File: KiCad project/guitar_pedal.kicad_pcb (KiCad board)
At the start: 2 copper layers, 46 parts, among them J1 NMJ6HCD2, J2 NMJ6HCD2, J3 AVR-ISP-6, SW2 SWITCH_3PDT, U1 ATmega1284-P, U2 L7805, U3 TL061, U4 TL061, Y1 Crystal 16MHz

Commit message: Minor changes to PCB
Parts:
- moved C4 38.5 mm to (66.0, 48.2), turned to 0 degrees
- moved C2 31.4 mm to (66.0, 43.1), turned to 0 degrees
- moved D1 27.0 mm to (71.1, 38.0), turned to 180 degrees
- moved R1 24.3 mm to (66.0, 38.0), turned to 0 degrees
- moved C18 19.5 mm to (71.1, 31.5), turned to 90 degrees
- moved C3 15.6 mm to (66.0, 31.5), turned to -90 degrees
- moved C1 14.6 mm to (61.0, 31.5), turned to -90 degrees
- moved U2 8.13 mm to (66.0, 25.3), turned to 0 degrees
- moved C15 5.24 mm to (61.0, 38.1), turned to 90 degrees
- moved C8 3.80 mm to (45.7, 76.1)
- moved R2 3.80 mm to (45.7, 81.2)
- moved R6 2.66 mm to (29.2, 68.6)
- moved R3 1.26 mm to (45.7, 71.1)
- moved C9 1.26 mm to (45.7, 65.9)
- moved J3 0.32 mm to (38.1, 38.1)
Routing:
- net +5V: track 10.9 -> 180.4 mm
- net Net-(U4--): track 29.1 -> 63.8 mm
- net GND: track 0.00 -> 21.4 mm
- net PA0: track 73.3 -> 92.3 mm
- net Net-(U3--): track 10.8 -> 8.08 mm
- net Net-(SW2-C2): track 38.0 -> 36.7 mm
- net Net-(U1-AREF): track 6.20 -> 7.33 mm
- net Net-(J3-SCK): track 15.4 -> 14.5 mm
- net Net-(U3-+): track 36.0 -> 36.6 mm
- net Net-(U1-XTAL2): track 18.4 -> 17.9 mm

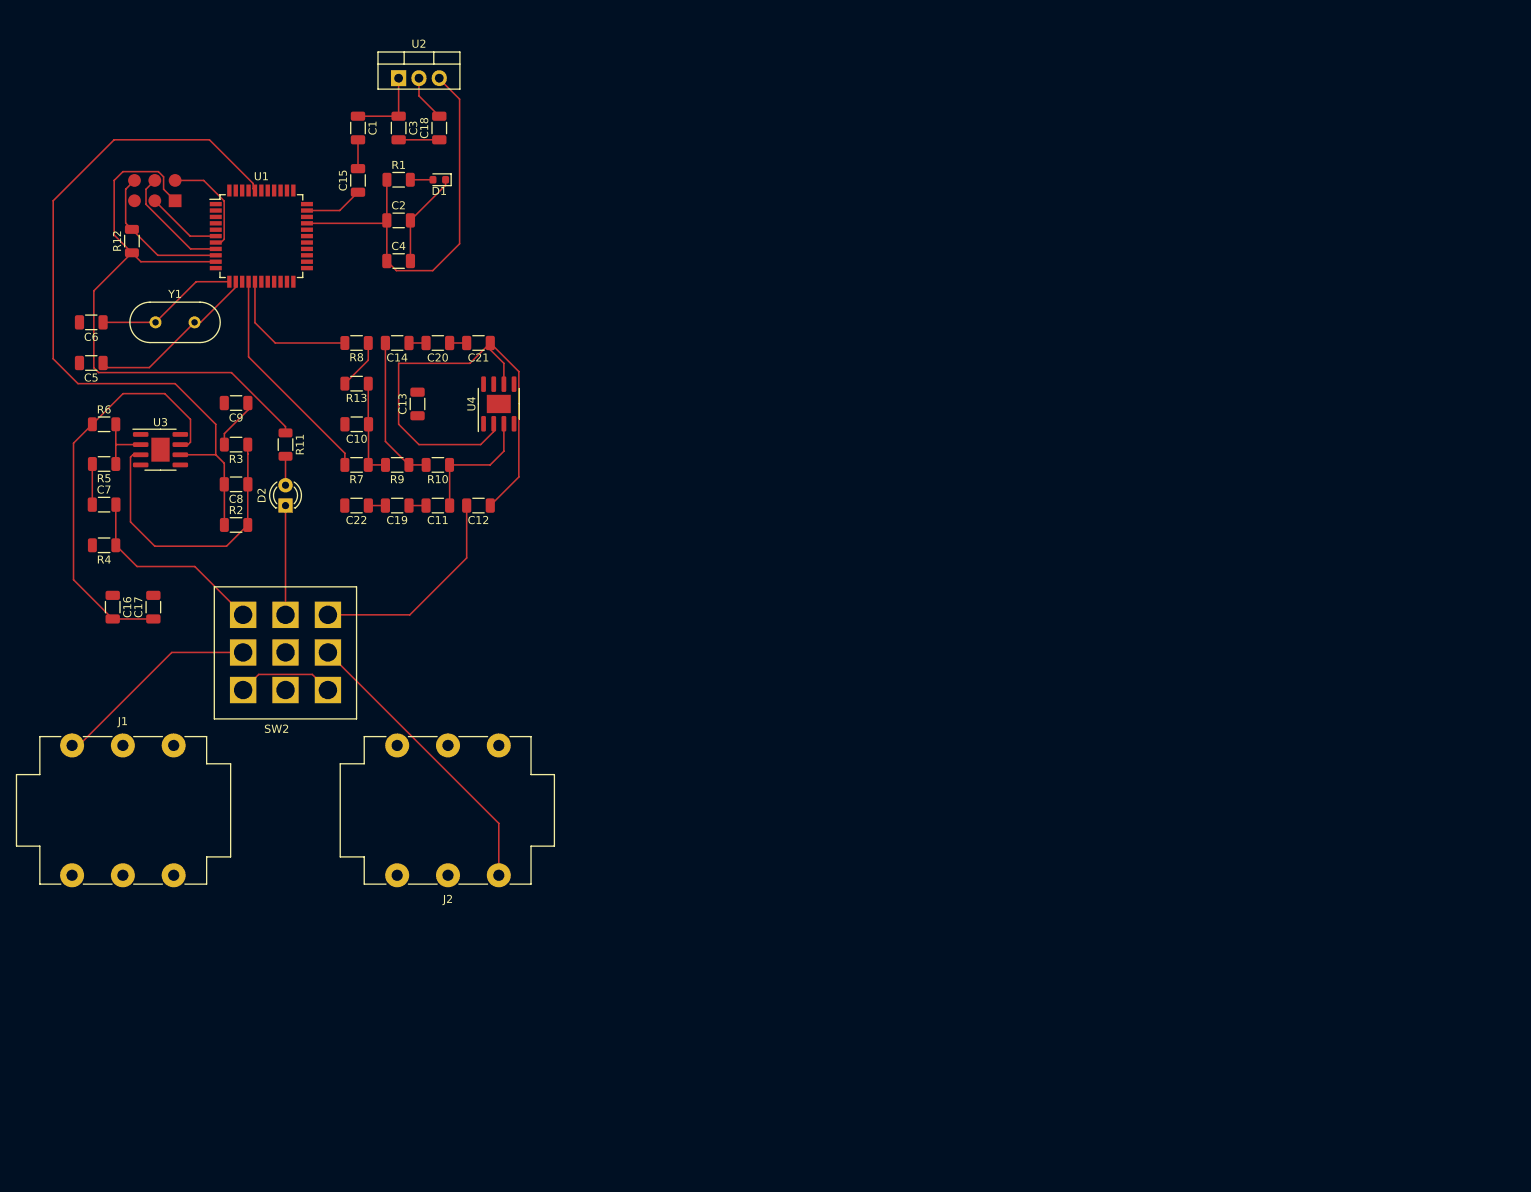
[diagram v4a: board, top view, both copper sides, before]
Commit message: Added remaining footprints to PCB, added ground plane and board edges.
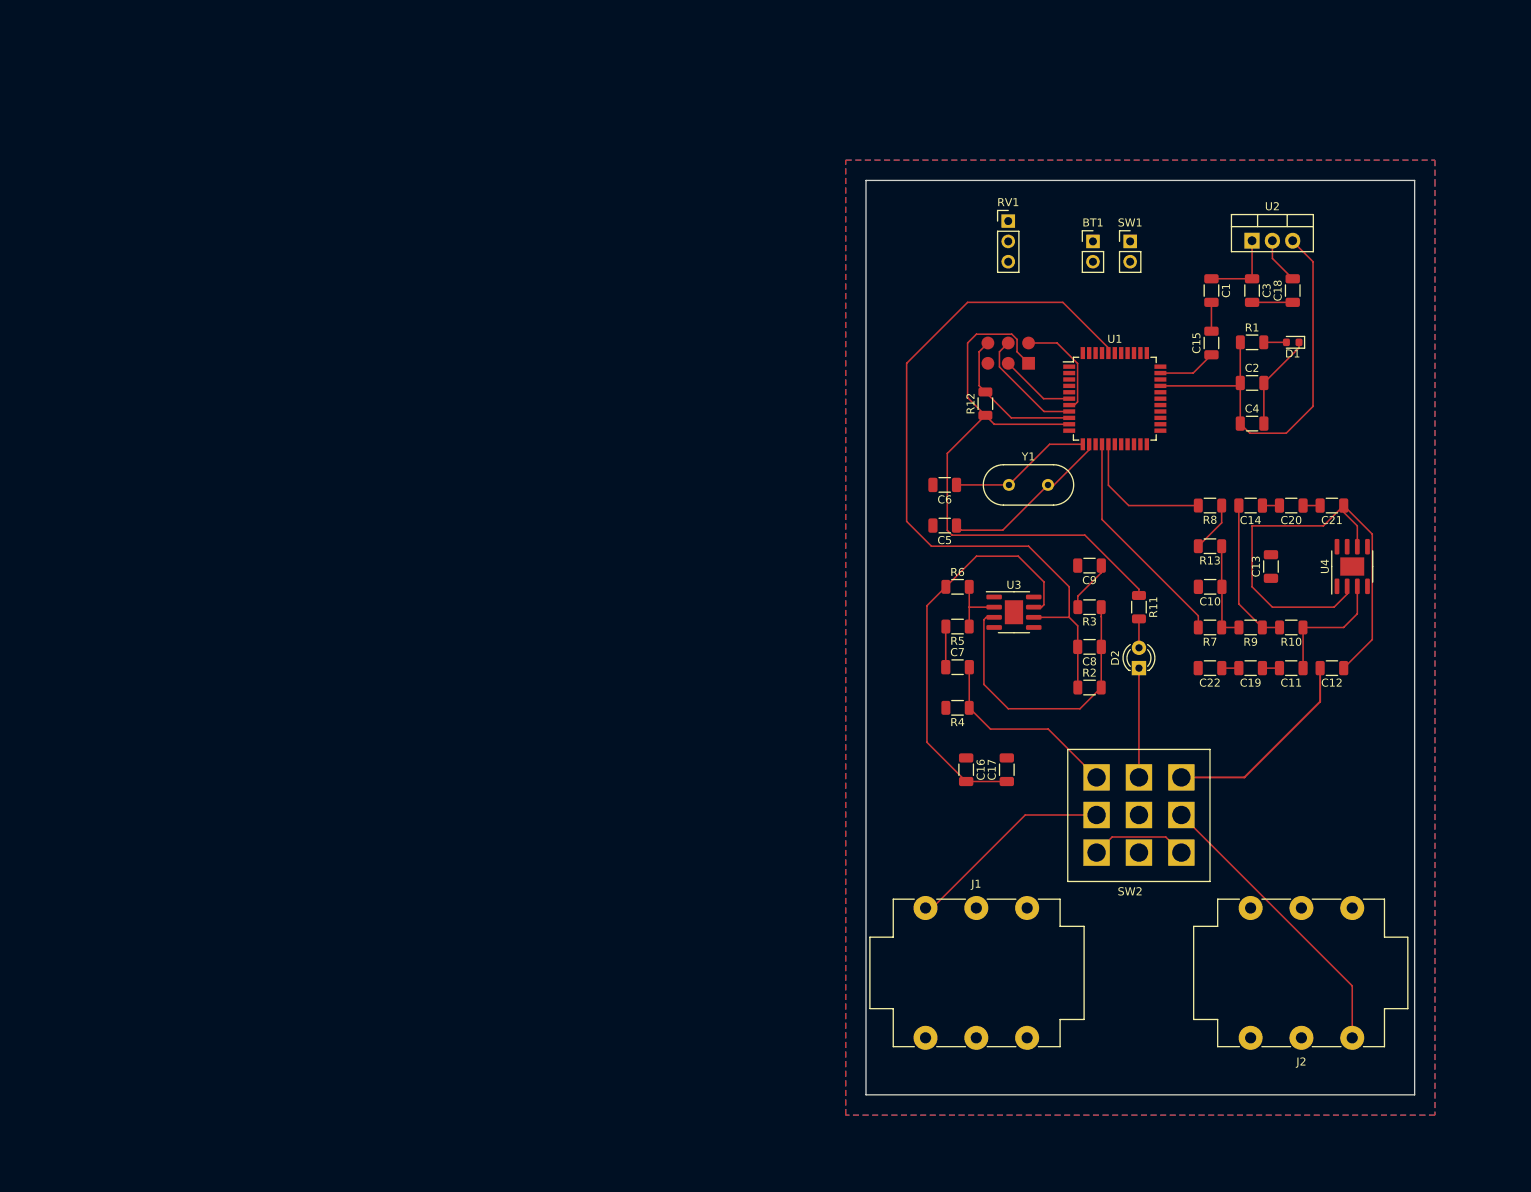
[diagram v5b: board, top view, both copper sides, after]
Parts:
- added BT1: 9V BATT, Connector_PinHeader_2.54mm:PinHeader_1x02_P2.54mm_Vertical, F.Cu at (152.8, 45.7)
- added RV1: R_Potentiometer, Connector_PinHeader_2.54mm:PinHeader_1x03_P2.54mm_Vertical, F.Cu at (142.2, 43.2)
- added SW1: SW_SPST, Connector_PinHeader_2.54mm:PinHeader_1x02_P2.54mm_Vertical, F.Cu at (157.5, 45.7)
- moved C11 108.6 mm to (177.6, 99.1)
- moved C13 108.6 mm to (175.1, 86.4)
- moved C17 108.6 mm to (142.1, 111.8)
- moved C18 108.6 mm to (177.8, 51.9)
- moved C20 108.6 mm to (177.6, 78.7)
- moved C22 108.6 mm to (167.5, 99.1)
- moved C5 108.6 mm to (134.3, 81.2)
- moved C6 108.6 mm to (134.3, 76.2)
- moved C7 108.6 mm to (135.9, 98.9)
- moved C8 108.6 mm to (152.4, 96.4)
- moved C9 108.6 mm to (152.4, 86.2)
- moved D1 108.6 mm to (177.8, 58.3)
- moved D2 108.6 mm to (158.6, 99.1)
- moved J1 108.6 mm to (131.9, 129.0)
- moved J2 108.6 mm to (185.2, 145.3)
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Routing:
- net FX Out: track 26.8 -> 25.5 mm
- added copper zone on B.Cu, net GND
- added copper zone on F.Cu, net GND
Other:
- board outline added: 68.6 x 114.3 mm

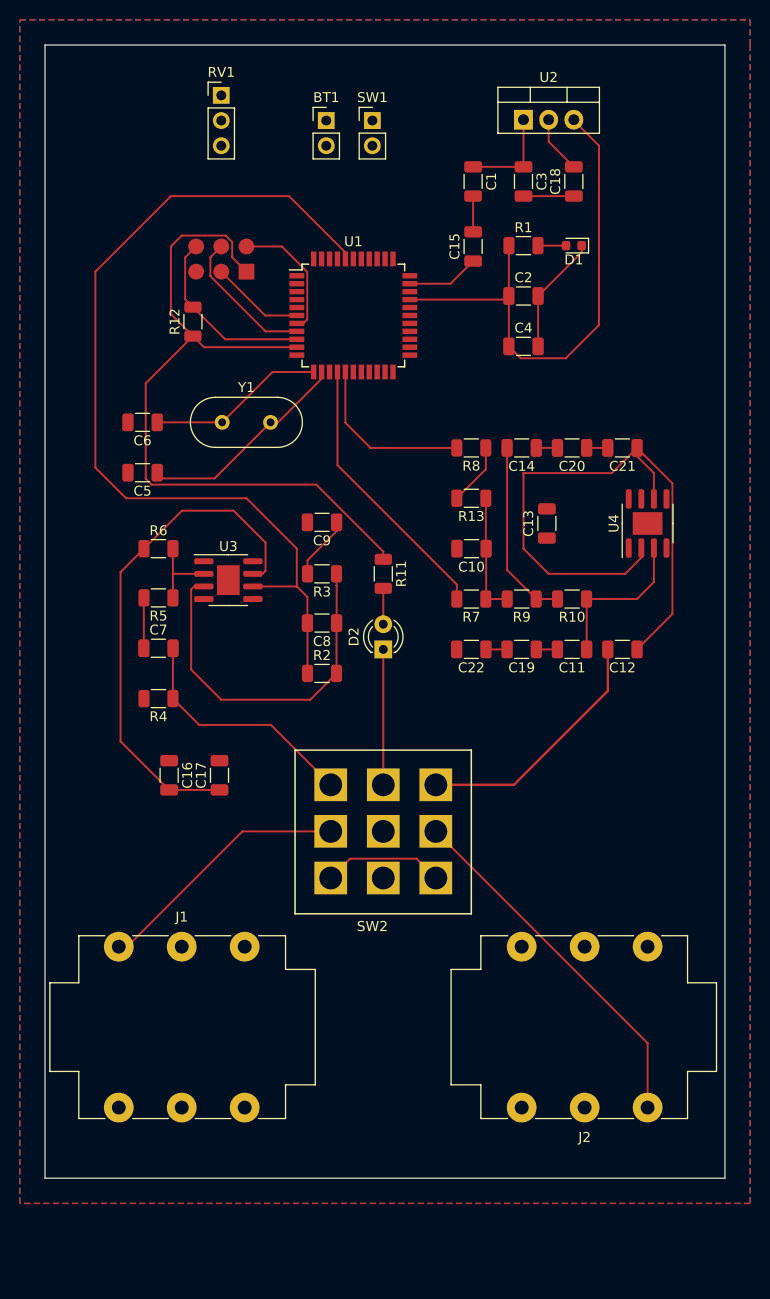
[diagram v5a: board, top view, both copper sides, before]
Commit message: Added second layer. All connections on board. No errors in DRC, 200+ warnings.
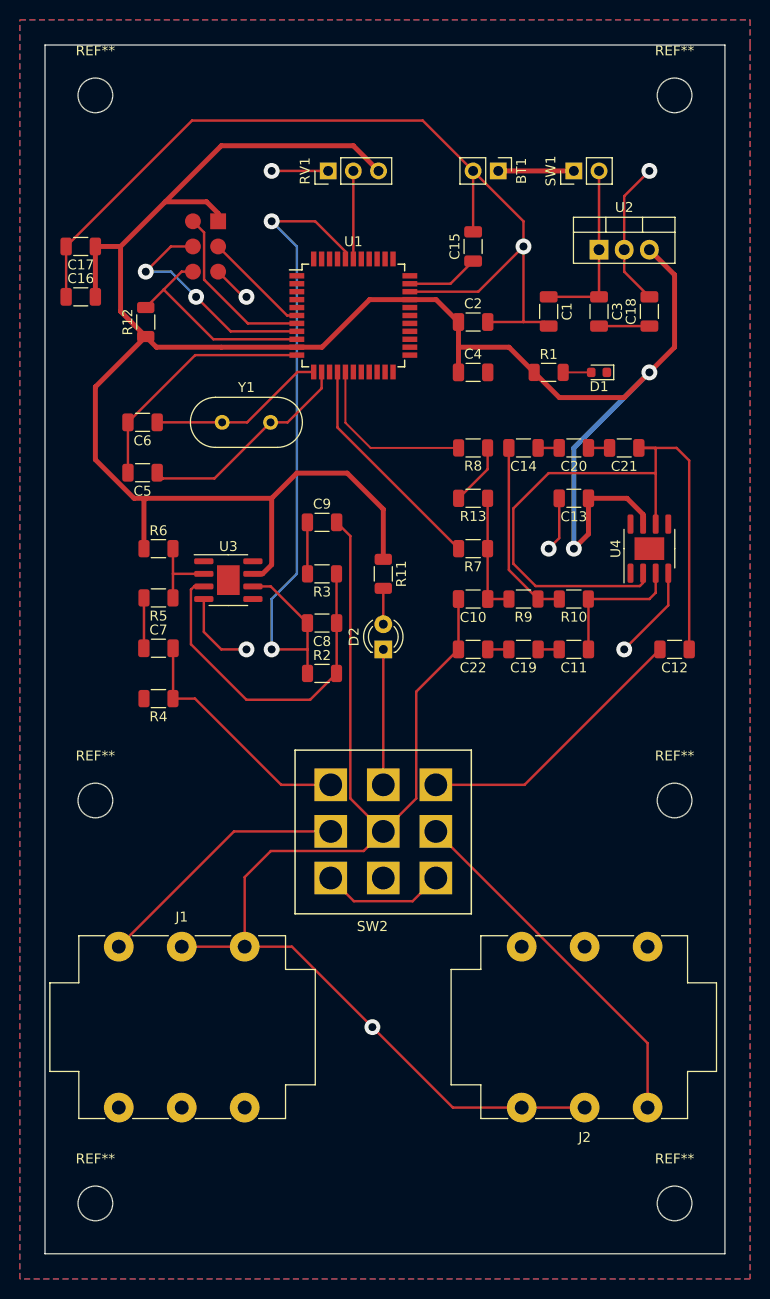
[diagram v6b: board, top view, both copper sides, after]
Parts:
- added REF**: MountingHole_3.5mm, MountingHole:MountingHole_3.5mm, F.Cu at (188.0, 114.3)
- added REF**: MountingHole_3.5mm, MountingHole:MountingHole_3.5mm, F.Cu at (188.0, 43.2)
- added REF**: MountingHole_3.5mm, MountingHole:MountingHole_3.5mm, F.Cu at (129.5, 43.2)
- added REF**: MountingHole_3.5mm, MountingHole:MountingHole_3.5mm, F.Cu at (129.5, 154.9)
- added REF**: MountingHole_3.5mm, MountingHole:MountingHole_3.5mm, F.Cu at (188.0, 154.9)
- added REF**: MountingHole_3.5mm, MountingHole:MountingHole_3.5mm, F.Cu at (129.5, 114.3)
- moved C17 55.1 mm to (128.1, 58.4), turned to 180 degrees
- moved C16 49.1 mm to (128.1, 63.5), turned to 0 degrees
- moved SW1 20.9 mm to (177.8, 50.8), turned to 90 degrees
- moved BT1 18.1 mm to (170.2, 50.8), turned to -90 degrees
- moved U2 15.2 mm to (180.3, 58.7)
- moved C1 15.2 mm to (175.3, 65.0)
- moved C3 15.2 mm to (180.3, 65.0)
- moved C18 15.2 mm to (185.4, 65.0)
- moved RV1 13.2 mm to (153.0, 50.8), turned to 90 degrees
- moved D1 13.0 mm to (180.3, 71.1)
- moved R1 13.0 mm to (175.3, 71.1)
- moved J3 5.97 mm to (139.4, 55.9), turned to 0 degrees
- moved C2 5.72 mm to (167.6, 66.0)
- moved C4 5.72 mm to (167.6, 71.1)
- moved C12 5.26 mm to (188.0, 99.1)
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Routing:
- net GND: track 21.4 -> 300.7 mm, vias 0 -> 8
- net +5V: track 180.4 -> 233.3 mm, vias 0 -> 2
- net PA0: track 92.3 -> 70.5 mm, vias 0 -> 2
- net Net-(J3-SCK): track 14.5 -> 23.5 mm, vias 0 -> 2
- net PA1: track 0.00 -> 8.88 mm
- net Net-(SW1-B): track 9.84 -> 17.8 mm
- net +9V: track 0.00 -> 7.62 mm
- net Net-(U4--): track 63.8 -> 70.6 mm
- net PD1: track 27.9 -> 22.9 mm
- net Net-(J3-MISO): track 13.2 -> 17.5 mm
- net Net-(J3-~{RST}): track 18.7 -> 21.8 mm
- net FX Out: track 25.5 -> 28.3 mm
- net Net-(U4-+): track 16.0 -> 14.1 mm
- net Net-(U3-+): track 36.6 -> 35.1 mm
- net Net-(J3-MOSI): track 9.45 -> 10.8 mm
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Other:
- board size 68.6 x 114.3 mm -> 68.6 x 121.9 mm

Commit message: Updates to silkscreen
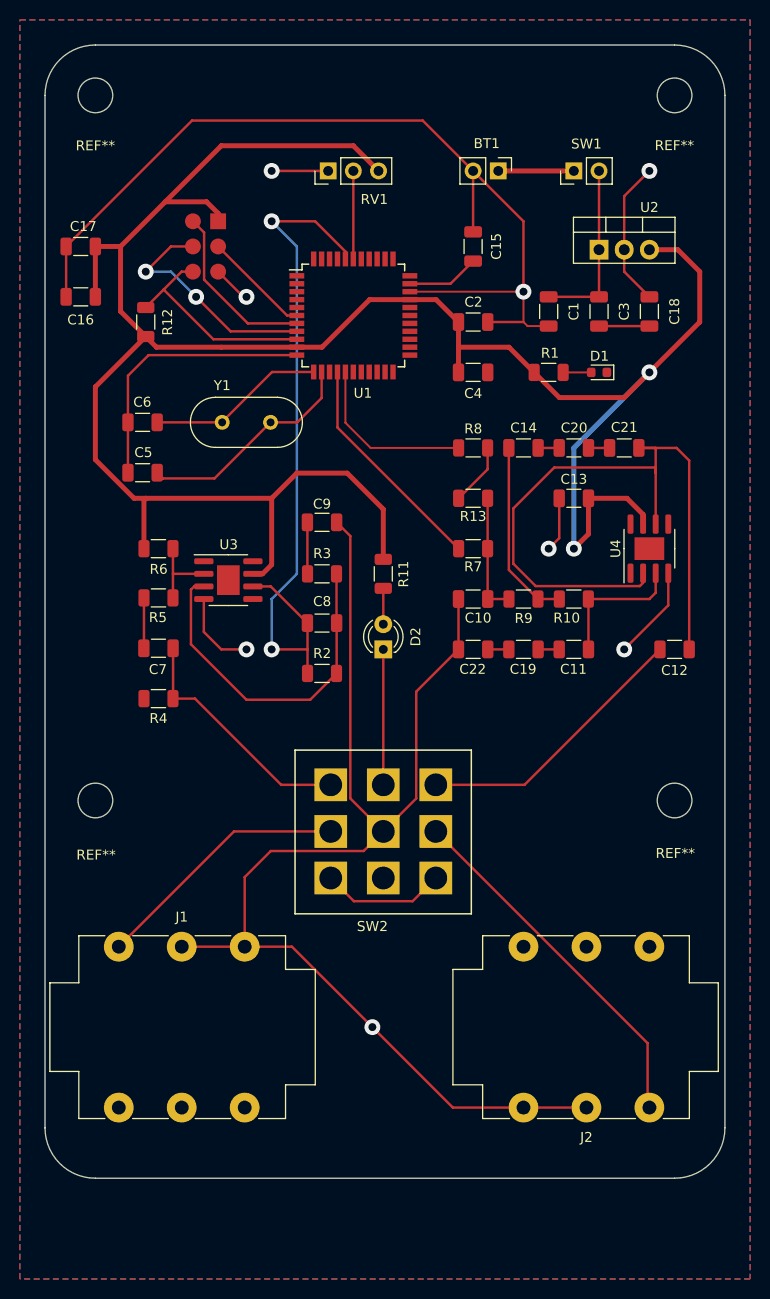
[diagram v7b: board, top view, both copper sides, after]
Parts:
- removed the REF** at (129.5, 154.9)
- removed the REF** at (188.0, 154.9)
- moved J2 0.18 mm to (185.4, 145.3)
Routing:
- net +5V: track 233.3 -> 237.0 mm
- net GND: track 300.7 -> 301.7 mm
- net Net-(U4--): track 70.6 -> 71.4 mm
- net Net-(U1-XTAL1): track 22.2 -> 22.8 mm
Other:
- board size 68.6 x 121.9 mm -> 68.6 x 114.3 mm

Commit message: Gerber files generated for 2 layer board.
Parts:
- added REF**: MountingHole_3.5mm, MountingHole:MountingHole_3.5mm, F.Cu at (155.0, 148.5)
- moved J1 4.41 mm to (128.3, 131.6)
- moved BT1 4.41 mm to (166.6, 53.3)
- moved C13 4.41 mm to (174.2, 86.4)
- moved C20 4.41 mm to (174.2, 81.3)
- moved C5 4.41 mm to (130.7, 83.8)
- moved C6 4.41 mm to (130.7, 78.7)
- moved R11 4.41 mm to (155.0, 94.0)
- moved R2 4.41 mm to (148.8, 104.0)
- moved R3 4.41 mm to (148.8, 94.0)
- moved REF** 4.41 mm to (184.4, 116.8)
- moved RV1 4.41 mm to (149.4, 53.3)
- moved SW1 4.41 mm to (174.2, 53.3)
- moved SW2 4.41 mm to (146.1, 111.8)
- moved Y1 4.41 mm to (138.7, 78.7)
- moved REF** 4.41 mm to (184.4, 45.7)
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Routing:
- net GND: track 301.7 -> 353.9 mm
